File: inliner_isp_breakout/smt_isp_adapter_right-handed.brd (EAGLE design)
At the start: 25.1 x 52.1 mm, 10 parts

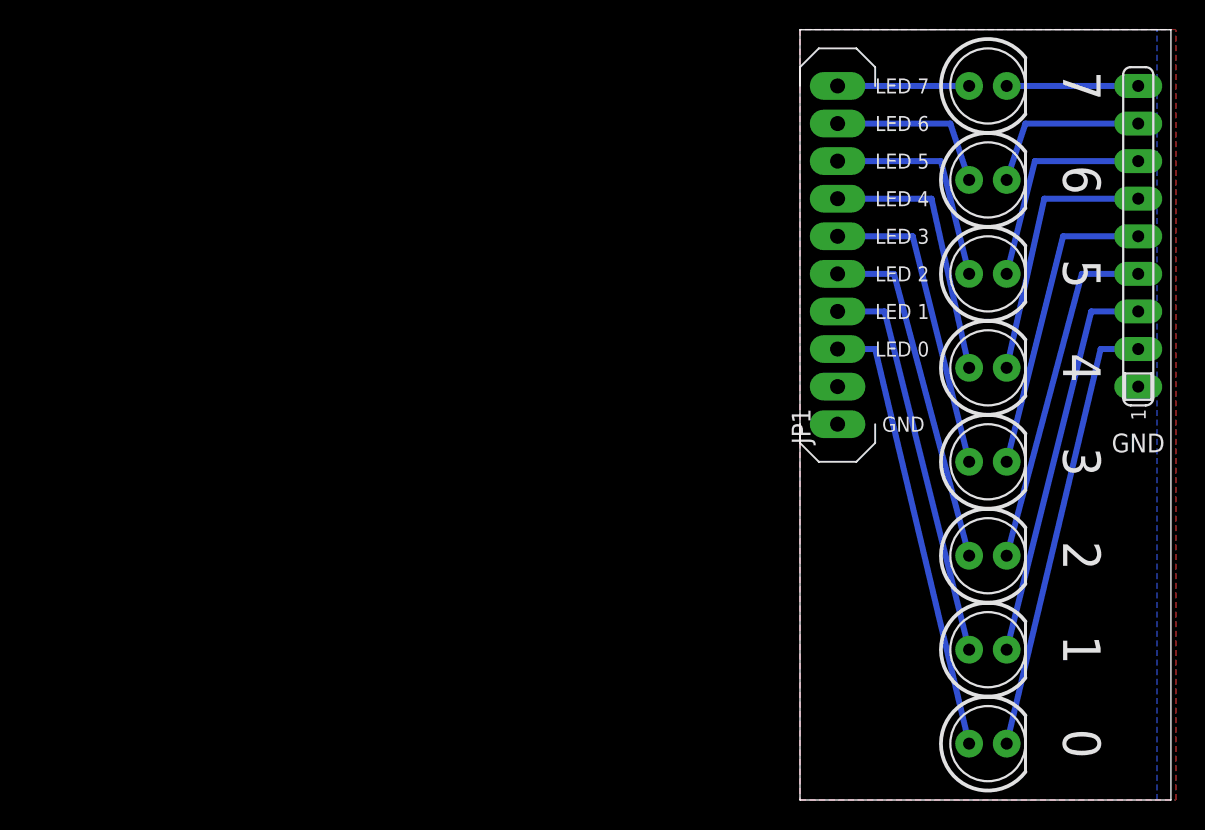
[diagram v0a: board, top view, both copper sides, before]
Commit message: added inliner, more top text
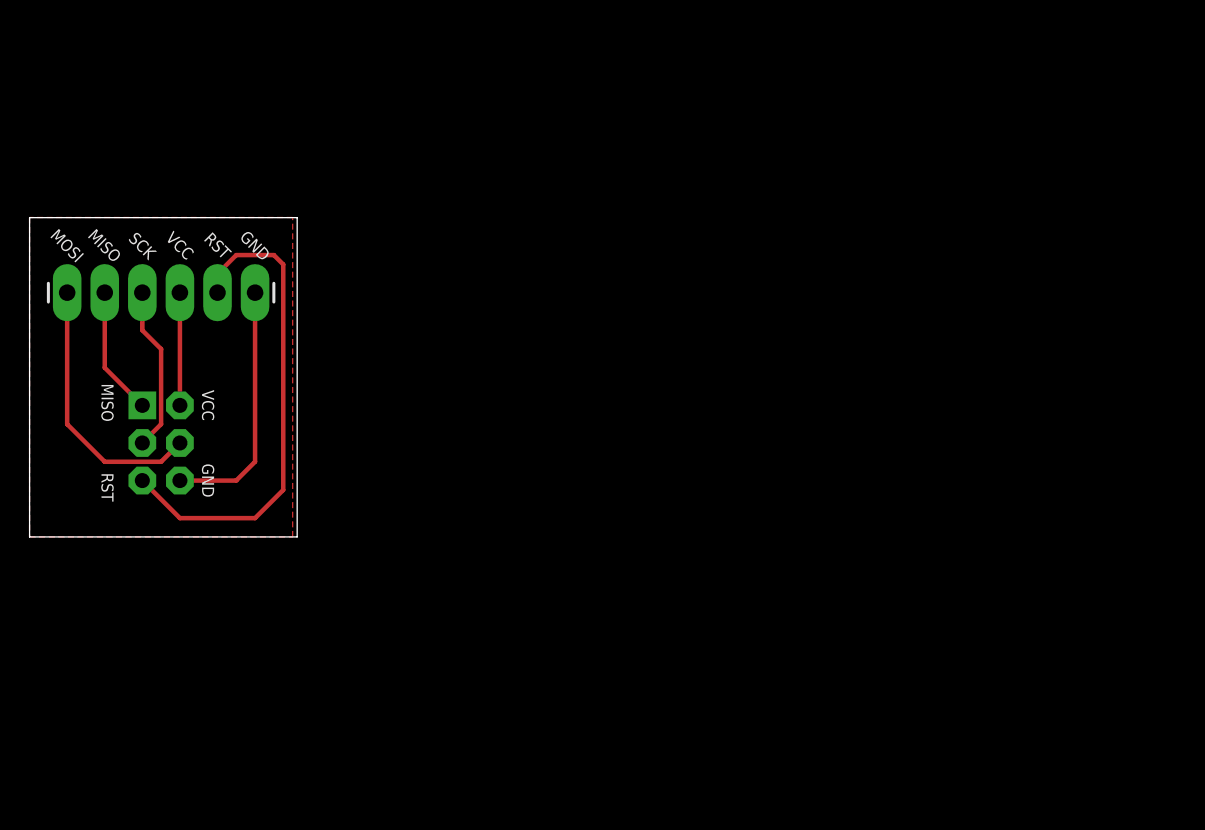
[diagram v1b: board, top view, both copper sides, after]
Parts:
- removed LED1, LED2, LED3, LED4, LED5, LED6, LED7, LED8: (no value), SparkFun-LED:LED5MM
- removed RN1: (no value), resistor-sil:SIL9
- added J2: AVR_SPI_PRG_6NS, SparkFun-Connectors:2X3-NS
- JP1: value M10" -> (none); device SparkFun-Connectors:1X10LONGPAD -> SparkFun-Connectors:1X06_LONGPADS
- moved JP1 40.4 mm to (21.6, 44.5), turned to 180 degrees
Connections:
- removed net N$1: LED1.K, RN1.9
- removed net N$10: JP1.9, LED2.A
- removed net N$11: JP1.8, LED3.A
- removed net N$12: JP1.7, LED4.A
- removed net N$13: JP1.6, LED5.A
- removed net N$14: JP1.5, LED6.A
- removed net N$15: JP1.4, LED7.A
- removed net N$16: JP1.3, LED8.A
- removed net N$2: LED2.K, RN1.8
- removed net N$3: LED3.K, RN1.7
- removed net N$4: LED4.K, RN1.6
- removed net N$5: LED5.K, RN1.5
- removed net N$6: LED6.K, RN1.4
- removed net N$7: LED7.K, RN1.3
- removed net N$8: LED8.K, RN1.2
- removed net N$9: JP1.10, LED1.A
- new net MISO: J2.1, JP1.5
- new net MOSI: J2.4, JP1.6
- new net RESET: J2.5, JP1.2
- new net SCK: J2.3, JP1.4
- new net VCC: J2.2, JP1.3
- net GND: now also J2.6; no longer RN1.1
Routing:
- net RESET: track 0.00 -> 33.1 mm
- net N$8: track 30.0 -> 0.00 mm
- net N$16: track 30.0 -> 0.00 mm
- net N$15: track 26.7 -> 0.00 mm
- net N$7: track 26.7 -> 0.00 mm
- net N$6: track 23.5 -> 0.00 mm
- net N$14: track 23.5 -> 0.00 mm
- net N$5: track 20.8 -> 0.00 mm
- net N$13: track 20.8 -> 0.00 mm
- net MOSI: track 0.00 -> 18.1 mm
- net N$12: track 18.1 -> 0.00 mm
- net N$4: track 18.1 -> 0.00 mm
- net GND: track 0.00 -> 17.0 mm
- net N$3: track 14.8 -> 0.00 mm
- net N$11: track 14.8 -> 0.00 mm
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- added copper zone on layer 1, net VCC
- removed copper zone on layer 1, net GND
- removed copper zone on layer 16, net GND
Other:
- board size 25.1 x 52.1 mm -> 18.1 x 21.6 mm
- board text added: "MISO"
- board text added: "MOSI"
- board text added: "RST"
- board text added: "SCK"
- board text added: "VCC"
- board text removed: "0"
- board text removed: "1"
- board text removed: "2"
- board text removed: "3"
- board text removed: "4"
- board text removed: "5"
- board text removed: "6"
- board text removed: "7"
- board text removed: "LED 0"
- board text removed: "LED 1"
- board text removed: "LED 2"
- board text removed: "LED 3"
- board text removed: "LED 4"
- board text removed: "LED 5"
- board text removed: "LED 6"
- board text removed: "LED 7"

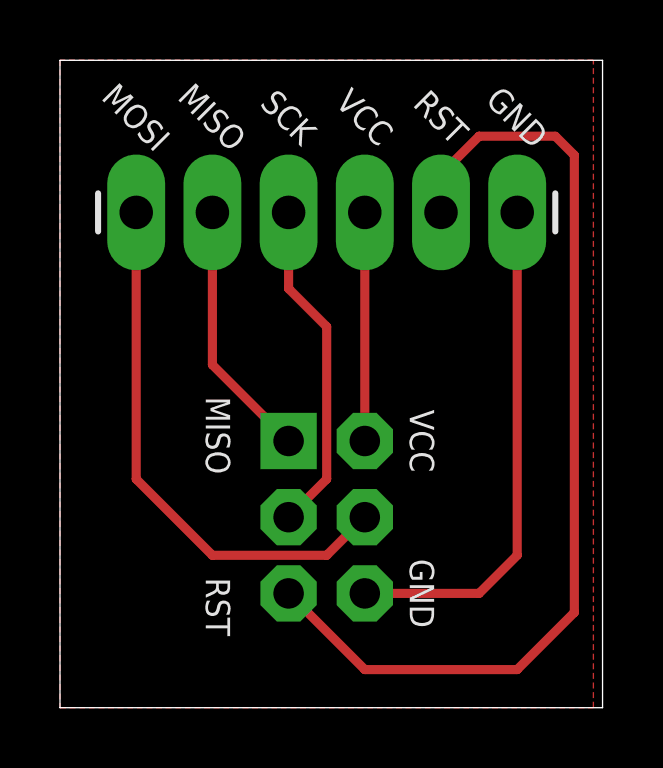
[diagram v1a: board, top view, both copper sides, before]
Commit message: added panelizing
first run-through using gerbmerge
there's a bunch of dirty details in panel.cfg
viewGerb is a quick script to open gerbers in the right order
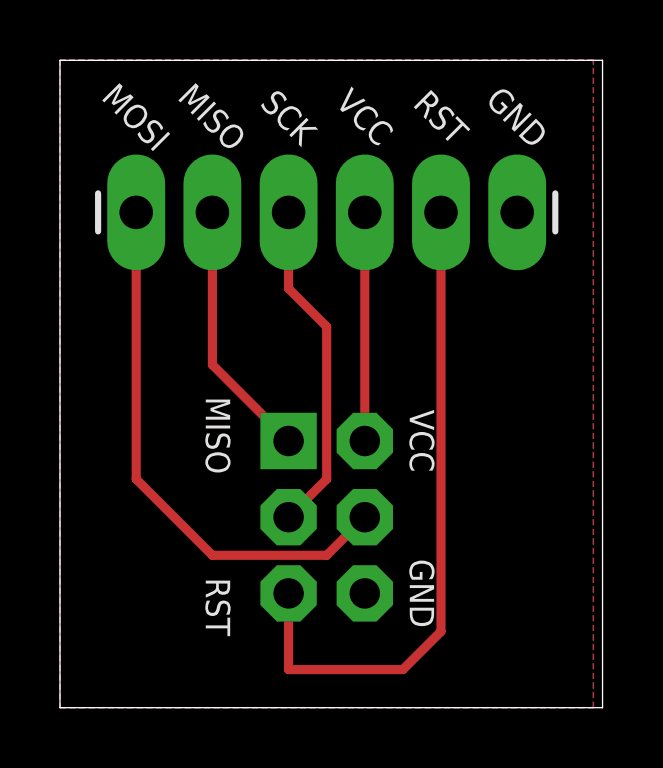
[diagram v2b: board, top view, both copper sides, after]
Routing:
- net GND: track 17.0 -> 0.00 mm
- net RESET: track 33.1 -> 22.1 mm
- added copper zone on layer 16, net GND
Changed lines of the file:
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@@
 <contactref element="JP1" pad="1"/>
 <contactref element="J2" pad="6"/>
-<wire x1="16.51" y1="31.75" x2="20.32" y2="31.75" width="0.3048" layer="1"/>
-<wire x1="20.32" y1="31.75" x2="21.59" y2="33.02" width="0.3048" layer="1"/>
-<wire x1="21.59" y1="33.02" x2="21.59" y2="44.45" width="0.3048" layer="1"/>
+<polygon width="0.8128" layer="16">
+<vertex x="6.35" y="49.53"/>
+<vertex x="6.35" y="27.94"/>
+<vertex x="24.13" y="27.94"/>
+<vertex x="24.13" y="49.53"/>
+</polygon>
 </signal>
 <signal name="RESET">
 <contactref element="JP1" pad="2"/>
 <contactref element="J2" pad="5"/>
-<wire x1="13.97" y1="31.75" x2="16.51" y2="29.21" width="0.3048" layer="1"/>
-<wire x1="16.51" y1="29.21" x2="21.59" y2="29.21" width="0.3048" layer="1"/>
-<wire x1="21.59" y1="29.21" x2="23.495" y2="31.115" width="0.3048" layer="1"/>
-<wire x1="23.495" y1="31.115" x2="23.495" y2="46.355" width="0.3048" layer="1"/>
-<wire x1="23.495" y1="46.355" x2="22.86" y2="46.99" width="0.3048" layer="1"/>
-<wire x1="22.86" y1="46.99" x2="20.32" y2="46.99" width="0.3048" layer="1"/>
-<wire x1="20.32" y1="46.99" x2="19.05" y2="45.72" width="0.3048" layer="1"/>
-<wire x1="19.05" y1="45.72" x2="19.05" y2="44.45" width="0.3048" layer="1"/>
+<wire x1="13.97" y1="31.75" x2="13.97" y2="29.21" width="0.3048" layer="1"/>
+<wire x1="13.97" y1="29.21" x2="17.78" y2="29.21" width="0.3048" layer="1"/>
+<wire x1="17.78" y1="29.21" x2="19.05" y2="30.48" width="0.3048" layer="1"/>
+<wire x1="19.05" y1="30.48" x2="19.05" y2="44.45" width="0.3048" layer="1"/>
 </signal>
 <signal name="VCC">
